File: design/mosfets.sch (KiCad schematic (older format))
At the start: 15 parts, among them Q1 IRFS7530, Q2 IRFS7530, Q3 IRFS7530, Q4 IRFS7530, Q5 IRFS7530, Q6 IRFS7530

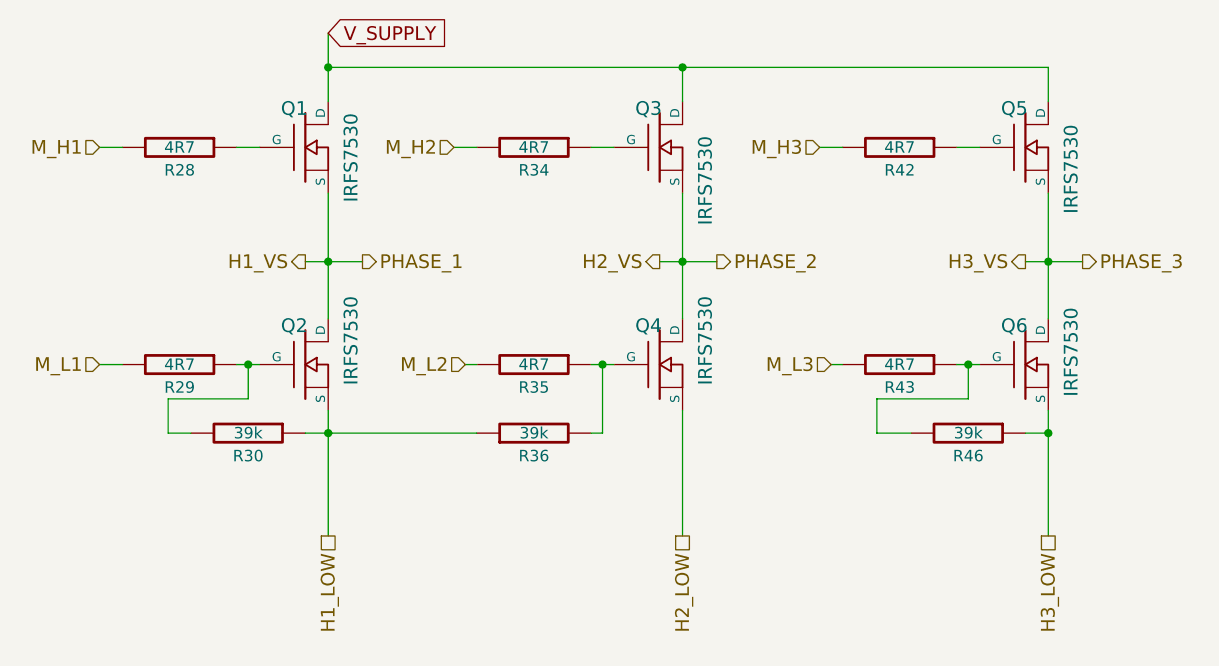
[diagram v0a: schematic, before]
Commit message: Implemented some improvements in schematic, but layout is completely new.
Changes in schematic:
- 3.3V or 5V CAN transceiver can be used
- DRV8301 can also be used and configured via SPI
- JTAG connector changed
- Fixed pinning of P1
- Some additional decoupling and/or filtering of analog signals
- Improved buck design according TI Webench recommendation
- Changed some component values
- maybe others...

Changes in layout:
- completely new layout
- placement of the big components is unchanged
- CAN connector rotated by 180°
- kept one layer free as a good GND plane
- many traces should be shorter and have lower impedance now
- improved buck layout

Other changes:
- updated gerber files
- updated PDFs (schematic and component placement)
- deleted all outdated files except libraries and datasheets
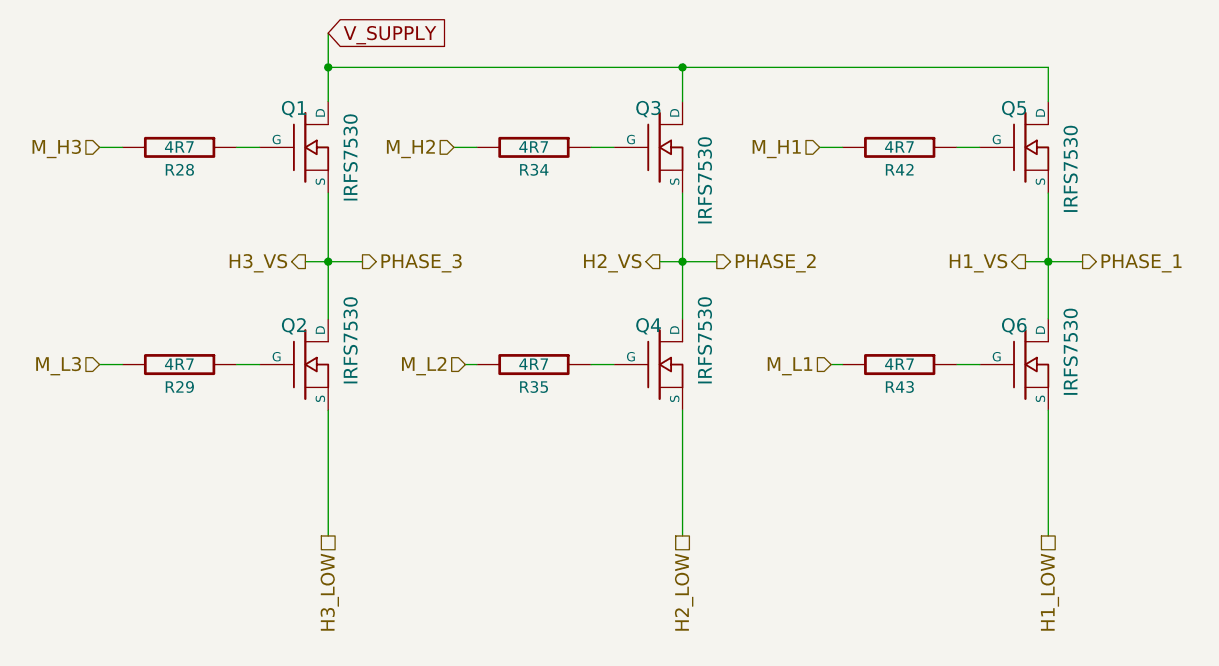
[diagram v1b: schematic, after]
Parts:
- removed R30, R36, R46: 39k, CRF1:SMD-0603_r, symbol R-RESCUE-BLDC_4
- Q1, Q2, Q3, Q4, Q5, Q6: footprint CRF1:D2PAK-7-GDS -> pikim:D2PAK-7-GDS
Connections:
- net H1_LOW: now also Q6.S; no longer Q2.S
- net H1_VS: now also Q5.S, Q6.D; no longer Q1.S, Q2.D
- net H3_LOW: now also Q2.S; no longer Q6.S
- net H3_VS: now also Q1.S, Q2.D; no longer Q5.S, Q6.D
- net M_H1: now also R42.2; no longer R28.2
- net M_H3: now also R28.2; no longer R42.2
- net M_L1: now also R43.2; no longer R29.2
- net M_L3: now also R29.2; no longer R43.2
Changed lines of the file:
@@
 EESchema Schematic File Version 2
-LIBS:BLDC_4-rescue
 LIBS:power
 LIBS:device
@@
 LIBS:contrib
 LIBS:valves
-LIBS:crf_1
 LIBS:BLDC_4-cache
 EELAYER 25 0
@@
 encoding utf-8
 Sheet 2 7
-Title "BLDC Driver 4.11"
-Date "21 aug 2015"
-Rev "4.11"
+Title "BLDC Driver 4.11p"
+Date "2016-01-06"
+Rev "A"
 Comp "Benjamin Vedder"
-Comment1 ""
+Comment1 "modified by pikim"
 Comment2 ""
 Comment3 ""
 Comment4 ""
 $EndDescr
-$Comp
-L R-RESCUE-BLDC_4 R46
-U 1 1 53F8E60B
-P 7850 4050
-F 0 "R46" V 7950 4050 50  0000 C CNN
-F 1 "39k" V 7850 4050 50  0000 C CNN
-F 2 "CRF1:SMD-0603_r" H 7850 4050 60  0001 C CNN
-F 3 "" H 7850 4050 60  0001 C CNN
-	1    7850 4050
-	0    1    1    0
-$EndComp
-$Comp
-L R-RESCUE-BLDC_4 R30
-U 1 1 53F8E612
-P 4700 4050
-F 0 "R30" V 4800 4050 50  0000 C CNN
-F 1 "39k" V 4700 4050 50  0000 C CNN
-F 2 "CRF1:SMD-0603_r" H 4700 4050 60  0001 C CNN
-F 3 "" H 4700 4050 60  0001 C CNN
-	1    4700 4050
-	0    1    1    0
-$EndComp
 $Comp
 L MOSFET_N Q1
@@
 F 0 "Q1" H 4960 2970 60  0000 R CNN
 F 1 "IRFS7530" V 5150 2950 60  0000 R CNN
-F 2 "CRF1:D2PAK-7-GDS" H 4950 2800 60  0001 C CNN
+F 2 "pikim:D2PAK-7-GDS" H 4950 2800 60  0001 C CNN
 F 3 "" H 4950 2800 60  0001 C CNN
 	1    4950 2800
@@
 F 0 "Q2" H 4960 3920 60  0000 R CNN
 F 1 "IRFS7530" V 5150 4050 60  0000 R CNN
-F 2 "CRF1:D2PAK-7-GDS" H 4950 3750 60  0001 C CNN
+F 2 "pikim:D2PAK-7-GDS" H 4950 3750 60  0001 C CNN
 F 3 "" H 4950 3750 60  0001 C CNN
 	1    4950 3750
@@
 F 0 "Q4" H 6510 3920 60  0000 R CNN
 F 1 "IRFS7530" V 6700 4050 60  0000 R CNN
-F 2 "CRF1:D2PAK-7-GDS" H 6500 3750 60  0001 C CNN
+F 2 "pikim:D2PAK-7-GDS" H 6500 3750 60  0001 C CNN
 F 3 "" H 6500 3750 60  0001 C CNN
 	1    6500 3750
@@
 F 0 "Q3" H 6510 2970 60  0000 R CNN
 F 1 "IRFS7530" V 6700 2850 60  0000 R CNN
-F 2 "CRF1:D2PAK-7-GDS" H 6500 2800 60  0001 C CNN
+F 2 "pikim:D2PAK-7-GDS" H 6500 2800 60  0001 C CNN
 F 3 "" H 6500 2800 60  0001 C CNN
 	1    6500 2800
@@
 F 0 "Q5" H 8110 2970 60  0000 R CNN
 F 1 "IRFS7530" V 8300 2900 60  0000 R CNN
-F 2 "CRF1:D2PAK-7-GDS" H 8100 2800 60  0001 C CNN
+F 2 "pikim:D2PAK-7-GDS" H 8100 2800 60  0001 C CNN
 F 3 "" H 8100 2800 60  0001 C CNN
 	1    8100 2800
@@
 F 0 "Q6" H 8110 3920 60  0000 R CNN
 F 1 "IRFS7530" V 8300 4000 60  0000 R CNN
-F 2 "CRF1:D2PAK-7-GDS" H 8100 3750 60  0001 C CNN
+F 2 "pikim:D2PAK-7-GDS" H 8100 3750 60  0001 C CNN
 F 3 "" H 8100 3750 60  0001 C CNN
 	1    8100 3750
@@
 	0    1    1    0
 $EndComp
-$Comp
-L R-RESCUE-BLDC_4 R36
-U 1 1 53F8E69C
-P 5950 4050
-F 0 "R36" V 5850 4050 50  0000 C CNN
-F 1 "39k" V 5950 4050 50  0000 C CNN
-F 2 "CRF1:SMD-0603_r" H 5950 4050 60  0001 C CNN
-F 3 "" H 5950 4050 60  0001 C CNN
-	1    5950 4050
-	0    -1   -1   0
-$EndComp
-Wire Wire Line
-	8100 4050 8200 4050
-Wire Wire Line
-	4950 4050 5700 4050
 Wire Wire Line
 	7250 3750 7300 3750
@@
 Wire Wire Line
 	5050 2450 8200 2450
-Wire Wire Line
-	7850 3750 7850 3900
-Wire Wire Line
-	7850 3900 7450 3900
-Wire Wire Line
-	7450 3900 7450 4050
-Wire Wire Line
-	7450 4050 7600 4050
-Connection ~ 7850 3750
-Connection ~ 8200 4050
-Connection ~ 5050 4050
-Connection ~ 6250 3750
-Wire Wire Line
-	6200 4050 6250 4050
-Wire Wire Line
-	6250 4050 6250 3750
 Text GLabel 5050 2300 2    60   Input ~ 0
 V_SUPPLY
@@
 	6600 3950 6600 4500
 Text HLabel 4050 2800 0    60   Input ~ 0
-M_H1
+M_H3
 Text HLabel 4050 3750 0    60   Input ~ 0
-M_L1
+M_L3
 Text HLabel 4950 3300 0    60   Output ~ 0
-H1_VS
+H3_VS
 Text HLabel 5600 2800 0    60   Input ~ 0
 M_H2
@@
 H2_VS
 Text HLabel 5050 4500 3    60   UnSpc ~ 0
-H1_LOW
+H3_LOW
 Text HLabel 6600 4500 3    60   UnSpc ~ 0
 H2_LOW
 Text HLabel 8200 4500 3    60   UnSpc ~ 0
-H3_LOW
+H1_LOW
 Text HLabel 8100 3300 0    60   Output ~ 0
-H3_VS
+H1_VS
 Text HLabel 7200 2800 0    60   Input ~ 0
-M_H3
+M_H1
 Text HLabel 7250 3750 0    60   Input ~ 0
-M_L3
+M_L1
 Text HLabel 5200 3300 2    60   Output ~ 0
-PHASE_1
+PHASE_3
 Text HLabel 6750 3300 2    60   Output ~ 0
 PHASE_2
 Text HLabel 8350 3300 2    60   Output ~ 0
-PHASE_3
+PHASE_1
 $Bitmap
 Pos 10150 5600
@@
 00 00 00 41 83 58 05 00 00 08 1A C4 2A 00 00 40 D0 20 56 01 00 00 82 06 B1 0A 00 00 10 34 88 55
 00 00 80 A0 41 AC 02 00 00 04 CD FF 03 15 B2 0E 9E 1D 9F E2 F2 00 00 00 00 49 45 4E 44 AE 42 60
-82 47
+82 40
 EndData
 $EndBitmap
-Connection ~ 4700 3750
-Wire Wire Line
-	4700 3750 4700 3900
-Wire Wire Line
-	4700 3900 4350 3900
-Wire Wire Line
-	4350 3900 4350 4050
-Wire Wire Line
-	4350 4050 4450 4050
 $EndSCHEMATC
